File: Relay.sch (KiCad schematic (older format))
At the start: 0 parts

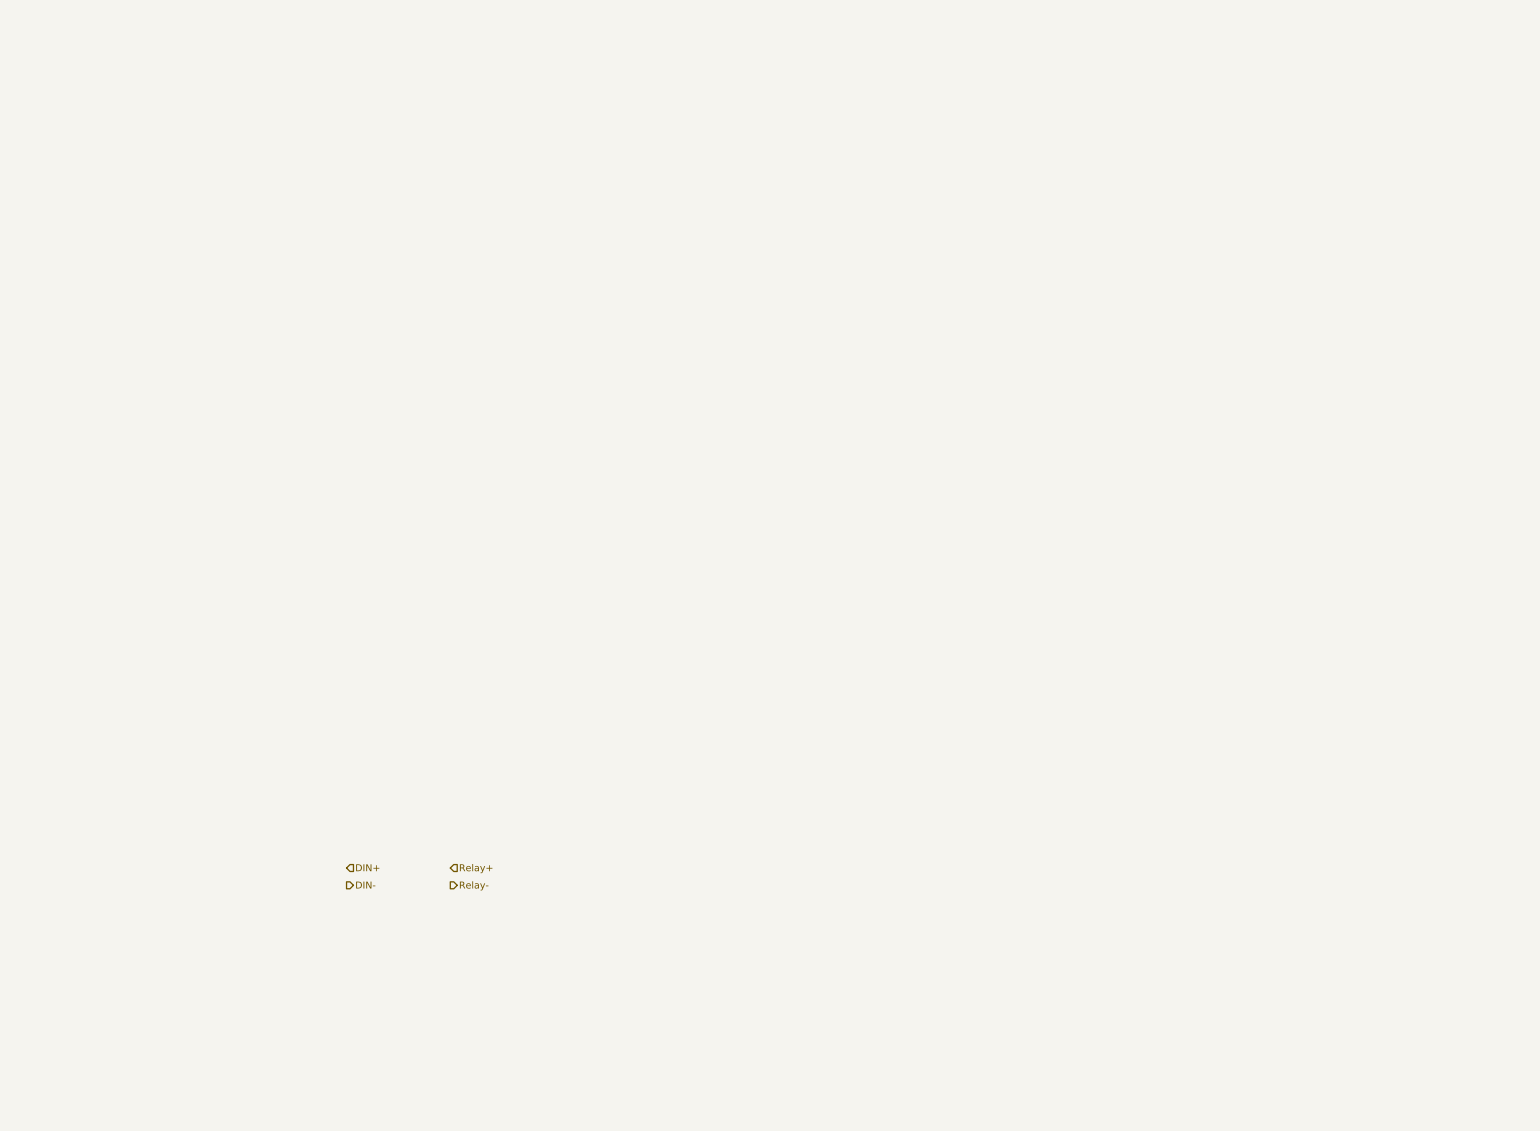
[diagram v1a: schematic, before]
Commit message: Relay Schematic
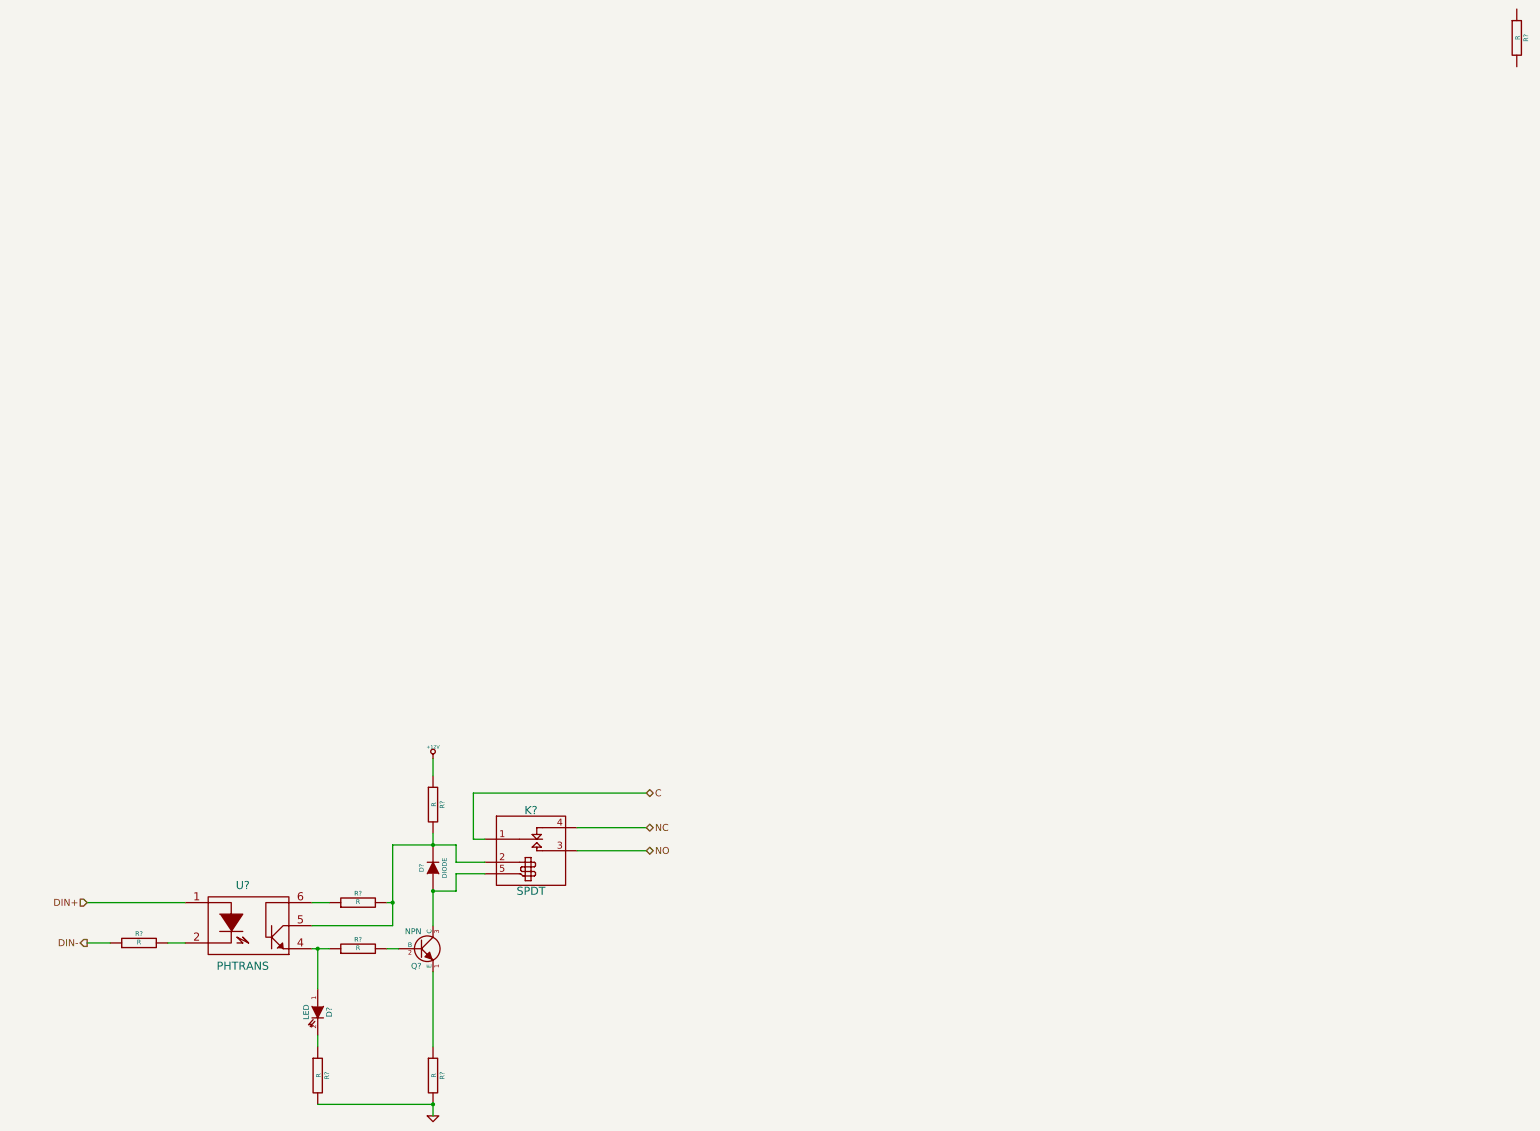
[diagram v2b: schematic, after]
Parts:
- added D?: DIODE, ~, symbol DIODE
- added D?: LED, ~, symbol LED
- added K?: SPDT, ~, symbol SPDT
- added Q?: NPN, ~, symbol NPN
- added R? (x7): R, ~, symbol R
- added U?: PHTRANS, ~, symbol PHTRANS
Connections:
- net DIN+: now also U?.1
- net DIN-: now also R?.1
- new net: D?.2 (K), K?.2 (COIL+), R?.2, R?.2, U?.5
- new net: D?.1 (A), K?.5 (COIL-), Q?.3 (C)
- new net: Q?.1 (E), R?.1
- new net: Q?.2 (B), R?.2
- new net: D?.2 (K), R?.1
- new net: R?.2, U?.2
- new net: D?.1 (A), R?.1, U?.4
- new net: R?.1, U?.6
- new net +12V: R?.1
- new net C: K?.1 (COM)
- new net GND: R?.2, R?.2
- new net NC: K?.4 (NC)
- new net NO: K?.3 (NO)
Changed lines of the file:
@@
 LIBS:contrib
 LIBS:valves
+LIBS:BenchBuddy
 LIBS:BenchBuddy-cache
 EELAYER 27 0
@@
 $Descr A4 11693 8268
 encoding utf-8
-Sheet 4 8
+Sheet 8 8
 Title ""
-Date "20 sep 2013"
+Date "21 sep 2013"
 Rev ""
 Comp ""
@@
 Comment4 ""
 $EndDescr
-Text HLabel 7000 3050 2    60   Input ~ 0
+Text HLabel 4750 3350 0    60   Input ~ 0
 DIN+
-Text HLabel 7000 3200 2    60   Output ~ 0
+Text HLabel 4750 3700 0    60   Output ~ 0
 DIN-
-Text HLabel 7900 3050 2    60   Input ~ 0
-Relay+
-Text HLabel 7900 3200 2    60   Output ~ 0
-Relay-
+Text HLabel 9600 2700 2    60   BiDi ~ 0
+NC
+Text HLabel 9600 2900 2    60   BiDi ~ 0
+NO
+$Comp
+L R R?
+U 1 1 523D0C55
+P 17150 -4150
+F 0 "R?" V 17230 -4150 40  0000 C CNN
+F 1 "R" V 17157 -4149 40  0000 C CNN
+F 2 "~" V 17080 -4150 30  0000 C CNN
+F 3 "~" H 17150 -4150 30  0000 C CNN
+	1    17150 -4150
+	1    0    0    -1
+$EndComp
+Text HLabel 9600 2400 2    60   BiDi ~ 0
+C
+$Comp
+L SPDT K?
+U 1 1 523D17C5
+P 8600 2750
+F 0 "K?" H 8600 2950 70  0000 C CNN
+F 1 "SPDT" H 8600 2250 70  0000 C CNN
+F 2 "~" H 8600 2750 60  0000 C CNN
+F 3 "~" H 8600 2750 60  0000 C CNN
+	1    8600 2750
+	1    0    0    -1
+$EndComp
+$Comp
+L NPN Q?
+U 1 1 523D17DC
+P 7650 3750
+F 0 "Q?" H 7650 3600 50  0000 R CNN
+F 1 "NPN" H 7650 3900 50  0000 R CNN
+F 2 "~" H 7650 3750 60  0000 C CNN
+F 3 "~" H 7650 3750 60  0000 C CNN
+	1    7650 3750
+	1    0    0    -1
+$EndComp
+$Comp
+L DIODE D?
+U 1 1 523D17F8
+P 7750 3050
+F 0 "D?" H 7750 3150 40  0000 C CNN
+F 1 "DIODE" H 7750 2950 40  0000 C CNN
+F 2 "~" H 7750 3050 60  0000 C CNN
+F 3 "~" H 7750 3050 60  0000 C CNN
+	1    7750 3050
+	0    -1   -1   0
+$EndComp
+$Comp
+L R R?
+U 1 1 523D1807
+P 6750 4850
+F 0 "R?" V 6830 4850 40  0000 C CNN
+F 1 "R" V 6757 4851 40  0000 C CNN
+F 2 "~" V 6680 4850 30  0000 C CNN
+F 3 "~" H 6750 4850 30  0000 C CNN
+	1    6750 4850
+	1    0    0    -1
+$EndComp
+$Comp
+L PHTRANS U?
+U 1 1 523D1825
+P 6150 3550
+F 0 "U?" H 6100 3900 70  0000 C CNN
+F 1 "PHTRANS" H 6100 3200 70  0000 C CNN
+F 2 "~" H 6150 3550 60  0000 C CNN
+F 3 "~" H 6150 3550 60  0000 C CNN
+	1    6150 3550
+	1    0    0    -1
+$EndComp
+$Comp
+L LED D?
+U 1 1 523D1884
+P 6750 4300
+F 0 "D?" H 6750 4400 50  0000 C CNN
+F 1 "LED" H 6750 4200 50  0000 C CNN
+F 2 "~" H 6750 4300 60  0000 C CNN
+F 3 "~" H 6750 4300 60  0000 C CNN
+	1    6750 4300
+	0    1    1    0
+$EndComp
+$Comp
+L R R?
+U 1 1 523D18B1
+P 7750 4850
+F 0 "R?" V 7830 4850 40  0000 C CNN
+F 1 "R" V 7757 4851 40  0000 C CNN
+F 2 "~" V 7680 4850 30  0000 C CNN
+F 3 "~" H 7750 4850 30  0000 C CNN
+	1    7750 4850
+	1    0    0    -1
+$EndComp
+$Comp
+L GND #PWR?
+U 1 1 523D18C2
+P 7750 5200
+F 0 "#PWR?" H 7750 5200 30  0001 C CNN
+F 1 "GND" H 7750 5130 30  0001 C CNN
+F 2 "" H 7750 5200 60  0000 C CNN
+F 3 "" H 7750 5200 60  0000 C CNN
+	1    7750 5200
+	1    0    0    -1
+$EndComp
+Wire Wire Line
+	8200 2800 8100 2800
+Wire Wire Line
+	8100 2800 8100 2400
+Wire Wire Line
+	8100 2400 9600 2400
+Wire Wire Line
+	9000 2700 9600 2700
+Wire Wire Line
+	9000 2900 9600 2900
+Wire Wire Line
+	7400 2850 7950 2850
+Wire Wire Line
+	7950 2850 7950 3000
+Wire Wire Line
+	7950 3000 8200 3000
+Wire Wire Line
+	8200 3100 7950 3100
+Wire Wire Line
+	7950 3100 7950 3250
+$Comp
+L +12V #PWR?
+U 1 1 523D1957
+P 7750 2100
+F 0 "#PWR?" H 7750 2050 20  0001 C CNN
+F 1 "+12V" H 7750 2200 30  0000 C CNN
+F 2 "" H 7750 2100 60  0000 C CNN
+F 3 "" H 7750 2100 60  0000 C CNN
+	1    7750 2100
+	1    0    0    -1
+$EndComp
+$Comp
+L R R?
+U 1 1 523D1A7F
+P 7100 3750
+F 0 "R?" V 7180 3750 40  0000 C CNN
+F 1 "R" V 7107 3751 40  0000 C CNN
+F 2 "~" V 7030 3750 30  0000 C CNN
+F 3 "~" H 7100 3750 30  0000 C CNN
+	1    7100 3750
+	0    -1   -1   0
+$EndComp
+Wire Wire Line
+	6700 3750 6850 3750
+Wire Wire Line
+	7350 3750 7450 3750
+Wire Wire Line
+	7750 3250 7750 3550
+Connection ~ 7750 3250
+Connection ~ 7750 5100
+Wire Wire Line
+	6750 5100 7750 5100
+Wire Wire Line
+	6750 4600 6750 4500
+Wire Wire Line
+	6750 4100 6750 3750
+Connection ~ 6750 3750
+Wire Wire Line
+	7750 3950 7750 4600
+$Comp
+L R R?
+U 1 1 523D1BDA
+P 7750 2500
+F 0 "R?" V 7830 2500 40  0000 C CNN
+F 1 "R" V 7757 2501 40  0000 C CNN
+F 2 "~" V 7680 2500 30  0000 C CNN
+F 3 "~" H 7750 2500 30  0000 C CNN
+	1    7750 2500
+	1    0    0    -1
+$EndComp
+Wire Wire Line
+	7750 2750 7750 2850
+Wire Wire Line
+	7750 2100 7750 2250
+Wire Wire Line
+	7750 5100 7750 5200
+Wire Wire Line
+	7950 3250 7750 3250
+Wire Wire Line
+	6700 3550 7400 3550
+Wire Wire Line
+	7400 3550 7400 2850
+Connection ~ 7750 2850
+$Comp
+L R R?
+U 1 1 523D1CFB
+P 7100 3350
+F 0 "R?" V 7180 3350 40  0000 C CNN
+F 1 "R" V 7107 3351 40  0000 C CNN
+F 2 "~" V 7030 3350 30  0000 C CNN
+F 3 "~" H 7100 3350 30  0000 C CNN
+	1    7100 3350
+	0    -1   -1   0
+$EndComp
+Wire Wire Line
+	6700 3350 6850 3350
+Wire Wire Line
+	7350 3350 7400 3350
+Connection ~ 7400 3350
+$Comp
+L R R?
+U 1 1 523D1D41
+P 5200 3700
+F 0 "R?" V 5280 3700 40  0000 C CNN
+F 1 "R" V 5207 3701 40  0000 C CNN
+F 2 "~" V 5130 3700 30  0000 C CNN
+F 3 "~" H 5200 3700 30  0000 C CNN
+	1    5200 3700
+	0    -1   -1   0
+$EndComp
+Wire Wire Line
+	5450 3700 5600 3700
+Wire Wire Line
+	4950 3700 4750 3700
+Wire Wire Line
+	4750 3350 5600 3350
 $EndSCHEMATC

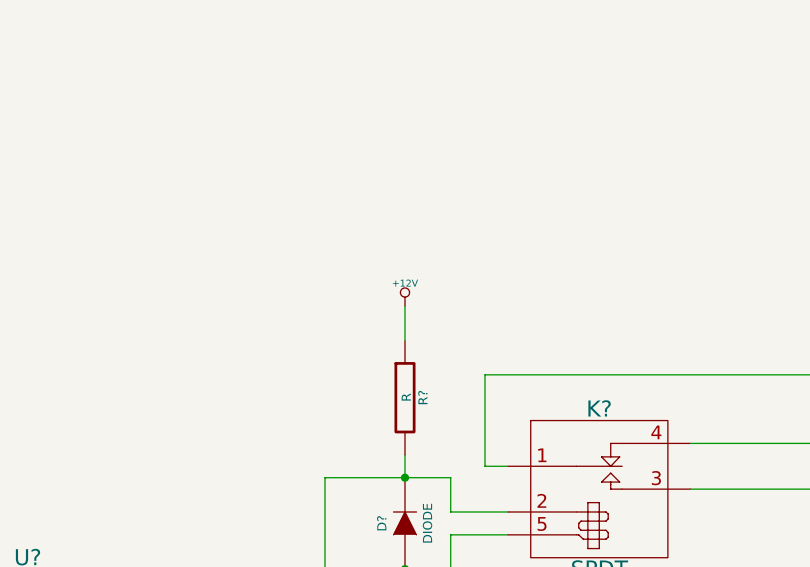
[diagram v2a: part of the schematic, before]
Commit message: Power Protection And Filtering
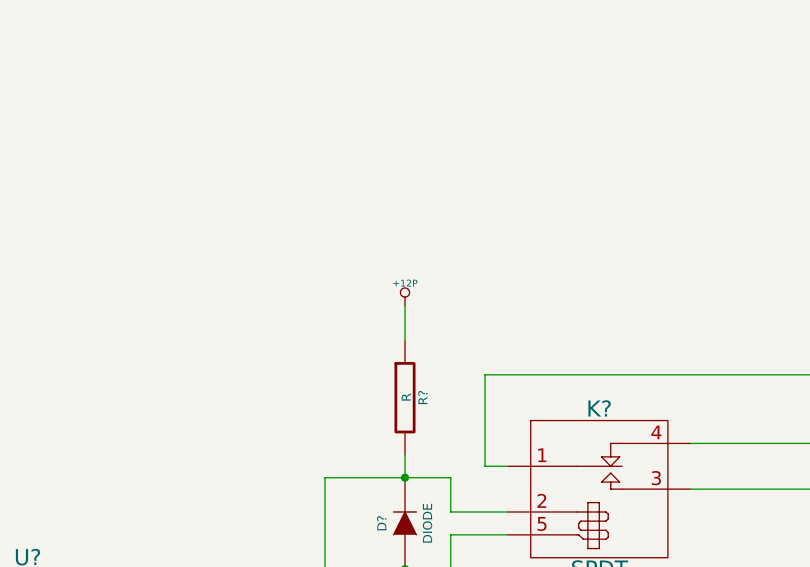
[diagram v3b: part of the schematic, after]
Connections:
- net +12V renamed +12P
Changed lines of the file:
@@
 $Descr A4 11693 8268
 encoding utf-8
-Sheet 8 8
+Sheet 8 9
 Title ""
-Date "21 sep 2013"
+Date "22 sep 2013"
 Rev ""
 Comp ""
@@
 	7950 3100 7950 3250
 $Comp
-L +12V #PWR?
-U 1 1 523D1957
-P 7750 2100
-F 0 "#PWR?" H 7750 2050 20  0001 C CNN
-F 1 "+12V" H 7750 2200 30  0000 C CNN
-F 2 "" H 7750 2100 60  0000 C CNN
-F 3 "" H 7750 2100 60  0000 C CNN
-	1    7750 2100
-	1    0    0    -1
-$EndComp
-$Comp
 L R R?
 U 1 1 523D1A7F
@@
 Wire Wire Line
 	4750 3350 5600 3350
+$Comp
+L +12P #PWR?
+U 1 1 523E67FE
+P 7750 2100
+F 0 "#PWR?" H 7750 2070 30  0001 C CNN
+F 1 "+12P" H 7750 2200 30  0000 C CNN
+F 2 "" H 7750 2100 60  0000 C CNN
+F 3 "" H 7750 2100 60  0000 C CNN
+	1    7750 2100
+	1    0    0    -1
+$EndComp
 $EndSCHEMATC

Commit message: Overall Schematic
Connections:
- net C renamed RELAY_COM
- net DIN+ renamed RELAY+
- net DIN- renamed RELAY-
- net NC renamed RELAY_NC
- net NO renamed RELAY_NO
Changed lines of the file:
@@
 $Descr A4 11693 8268
 encoding utf-8
-Sheet 8 9
+Sheet 7 9
 Title ""
-Date "22 sep 2013"
+Date "28 sep 2013"
 Rev ""
 Comp ""
@@
 $EndDescr
 Text HLabel 4750 3350 0    60   Input ~ 0
-DIN+
+RELAY+
 Text HLabel 4750 3700 0    60   Output ~ 0
-DIN-
+RELAY-
 Text HLabel 9600 2700 2    60   BiDi ~ 0
-NC
+RELAY_NC
 Text HLabel 9600 2900 2    60   BiDi ~ 0
-NO
+RELAY_NO
 $Comp
 L R R?
@@
 $EndComp
 Text HLabel 9600 2400 2    60   BiDi ~ 0
-C
+RELAY_COM
 $Comp
 L SPDT K?
